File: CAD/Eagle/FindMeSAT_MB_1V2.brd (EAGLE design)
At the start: 99 x 49.2 mm, 135 parts, among them Q101 ABS07-32.768KHZ, Q651 ABM3B-16MHZ-10-R50-1-U, U1001 CFPT-141-20MHZ, U101 ATXMEGA256A3BU-AU, U1011 OPA354, U1021 OPA354, U1111 LM2831YMF, U1121 LM4120IM5-3.0, U201 SIM808, U301 MPU-9250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

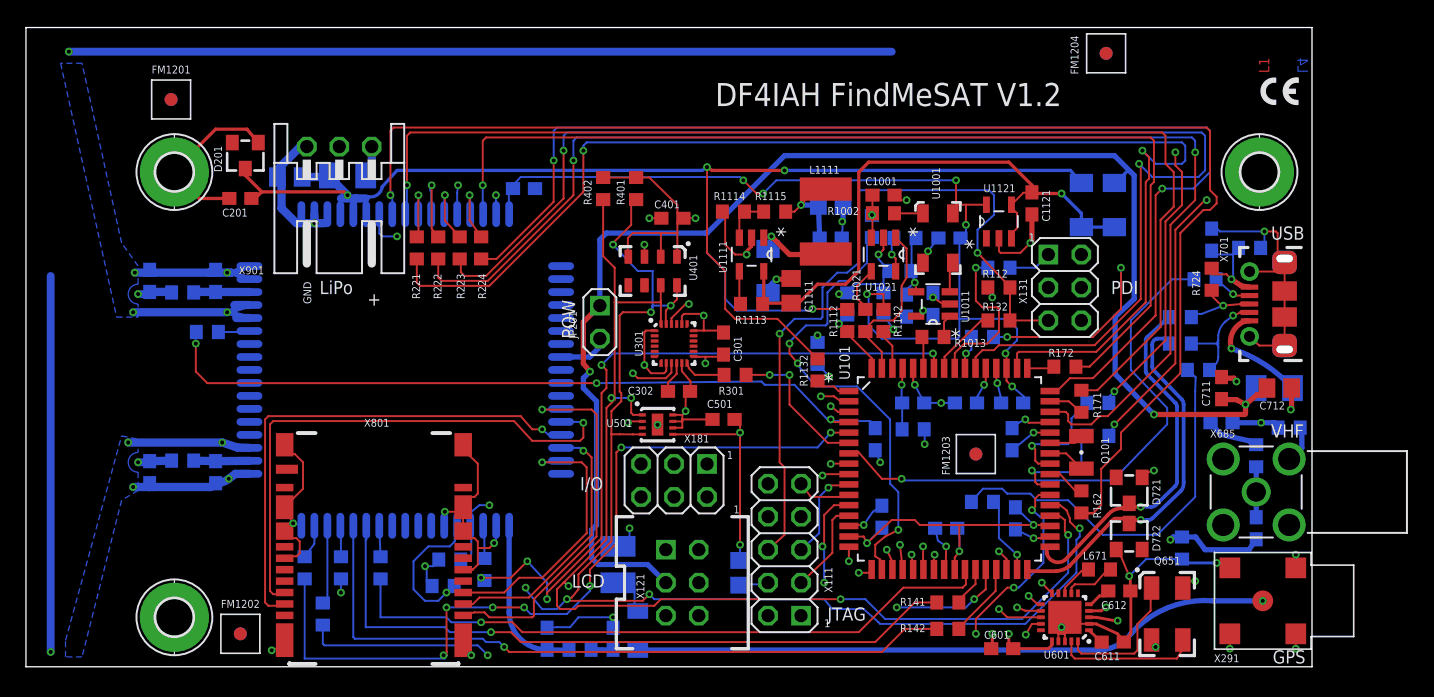
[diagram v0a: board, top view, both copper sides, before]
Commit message: HW_V1.2 - GSM antenna dimension (ADS), miter at busses, wire width in respect to 0.120 mm prepreg height - BT antenna still to do
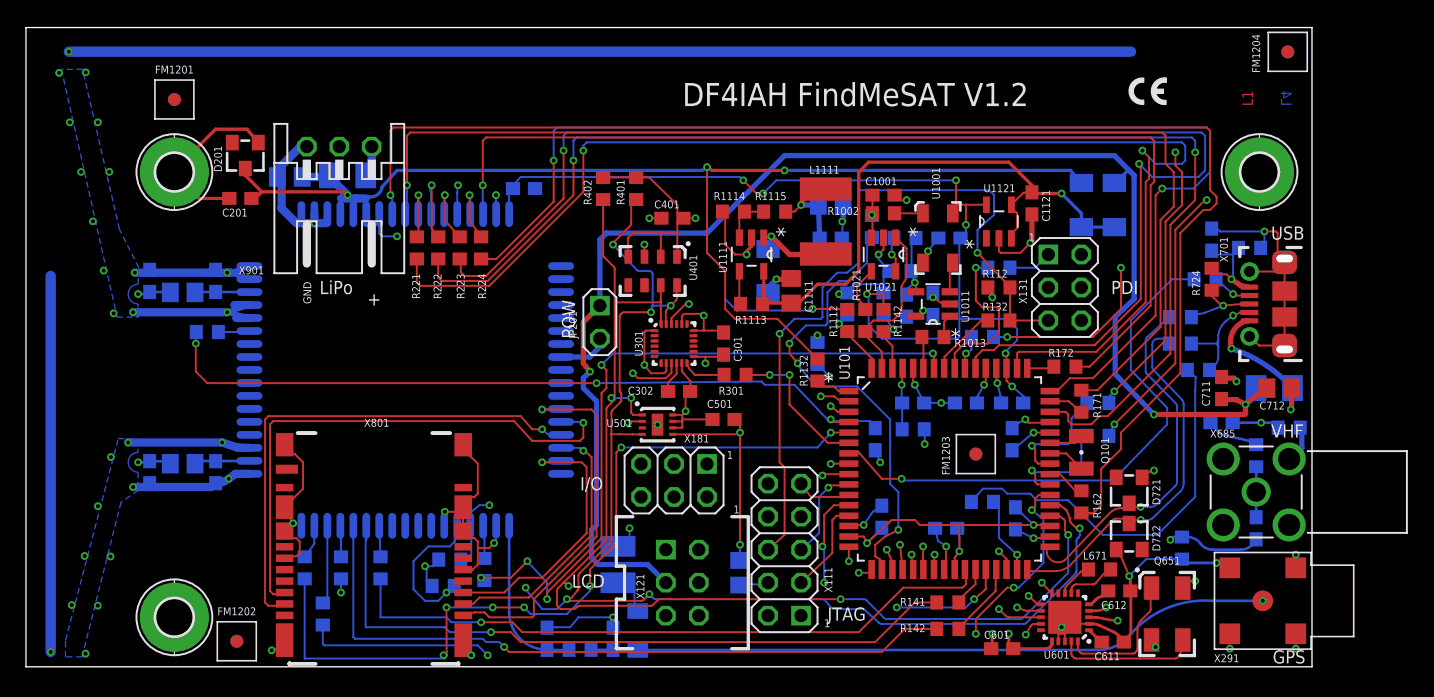
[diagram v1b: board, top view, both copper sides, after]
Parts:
- R271, R281: device rcl:R0603 -> rcl:R0805
- moved FM1204 14.0 mm to (97.2, 47.4)
- moved FM1202 0.64 mm to (16.2, 1.97)
- moved FM1201 0.25 mm to (11.4, 43.7)
- moved R281 0.24 mm to (12.1, 15.6)
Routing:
- net GSM_ANT: track 86.3 -> 104.8 mm
- net AX_CLK: track 14.4 -> 15.9 mm
- net SCL1: track 117.3 -> 116.4 mm
- net AX_ANTN: track 17.0 -> 16.5 mm
- net GND: vias 53 -> 69

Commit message: HW_V1.2 - GSM and BT antenna now without grounded arms
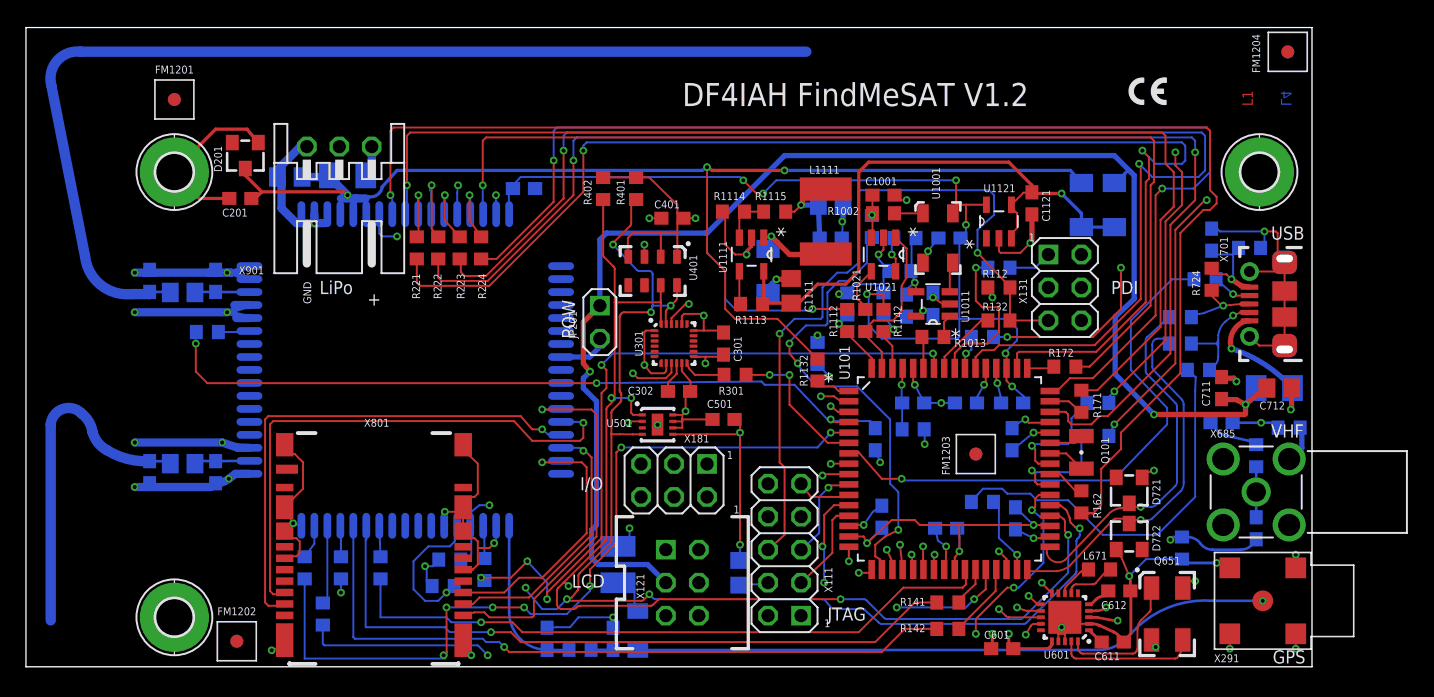
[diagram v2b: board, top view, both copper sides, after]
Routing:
- net GSM_ANT: track 104.8 -> 80.9 mm, vias 2 -> 0
- net BT_ANT: track 48.7 -> 26.2 mm, vias 2 -> 0
- net GND: track 233.1 -> 232.3 mm, vias 69 -> 53
- removed copper zone on layer 16, net GND
- removed copper zone on layer 2, net GND
- removed copper zone on layer 2, net SHIELD_BT
- removed copper zone on layer 2, net SHIELD_GSM

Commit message: HW_V1.2 - Eagle design made ready for the PCB board house
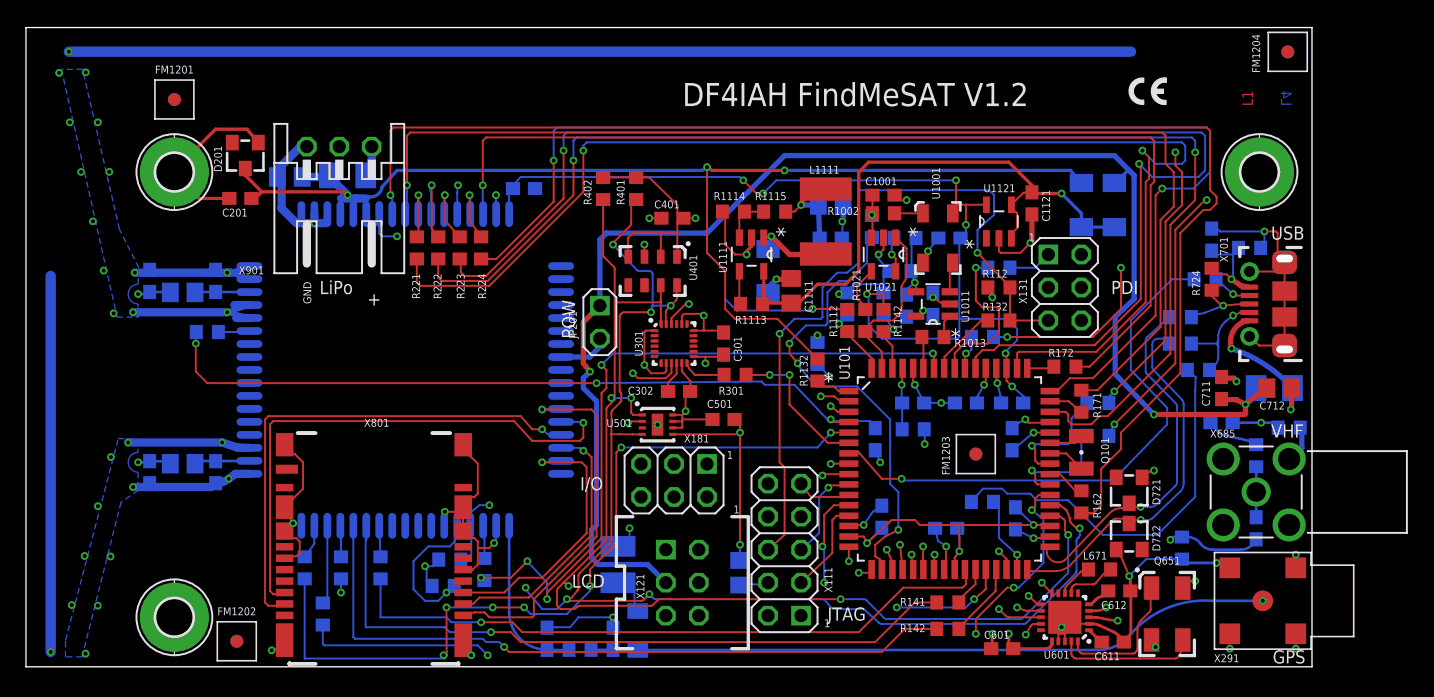
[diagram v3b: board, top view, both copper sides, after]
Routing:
- net GSM_ANT: track 80.9 -> 104.8 mm, vias 0 -> 2
- net BT_ANT: track 26.2 -> 48.7 mm, vias 0 -> 2
- net GND: track 232.3 -> 233.1 mm, vias 53 -> 69
- added copper zone on layer 16, net GND
- added copper zone on layer 2, net GND
- added copper zone on layer 2, net N$1
- added copper zone on layer 2, net N$2
- added copper zone on layer 2, net N$3
- added copper zone on layer 2, net N$4
- added copper zone on layer 2, net SHIELD_BT
- added copper zone on layer 2, net SHIELD_GSM

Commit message: HW_V1.2 - PWM low pass filter needs 10uF instead of 100nF, ADC measuring levels are 2.0V
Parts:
- C1001: value 100nF -> 10uF
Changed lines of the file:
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@@
 <attribute name="VALUE" x="71.755" y="31.115" size="1.27" layer="28" rot="MR0"/>
 </element>
-<element name="C1001" library="rcl" package="C0603" value="100nF" x="66.04" y="36.322" smashed="yes">
+<element name="C1001" library="rcl" package="C0603" value="10uF" x="66.04" y="36.322" smashed="yes">
 <attribute name="NAME" x="64.643" y="37.084" size="0.6096" layer="25"/>
 <attribute name="VALUE" x="65.278" y="35.941" size="0.6096" layer="27"/>

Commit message: HW_V1.2 - OPA354 needs higher comparator voltage for 50% duty cycle
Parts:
- R1012: value 470kR -> 270kR
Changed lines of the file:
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@@
 <attribute name="VALUE" x="69.469" y="27.432" size="0.6096" layer="28" rot="MR90"/>
 </element>
-<element name="R1012" library="rcl" package="R0603" value="470kR" x="67.691" y="33.02" smashed="yes" rot="MR0">
+<element name="R1012" library="rcl" package="R0603" value="270kR" x="67.691" y="33.02" smashed="yes" rot="MR0">
 <attribute name="NAME" x="68.961" y="33.909" size="0.6096" layer="26" rot="MR0"/>
 <attribute name="VALUE" x="68.453" y="32.766" size="0.6096" layer="28" rot="MR0"/>

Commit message: HW_V1.2 - Polyfuse of USB - value changed from 0.5A/1.0A to 1.1A/2.2A
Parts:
- RPOLY711: value 0.5A/1.0A -> 1.1A/2.2A
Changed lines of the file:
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@@
 <element name="H1203" library="holes" package="2,8-PAD" value="MOUNT-PAD-ROUND2.8" x="11.43" y="38.1" rot="R180"/>
 <element name="H1201" library="holes" package="2,8-PAD" value="MOUNT-PAD-ROUND2.8" x="94.996" y="38.1" smashed="yes" rot="R180"/>
-<element name="RPOLY711" library="rcl" package="M1206" value="0.5A/1.0A" x="96.139" y="21.463" smashed="yes" rot="MR0">
+<element name="RPOLY711" library="rcl" package="M1206" value="1.1A/2.2A" x="96.139" y="21.463" smashed="yes" rot="MR0">
 <attribute name="NAME" x="98.298" y="22.86" size="0.6096" layer="26" rot="MR0"/>
 <attribute name="VALUE" x="96.647" y="21.082" size="0.6096" layer="28" rot="MR0"/>

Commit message: HW_V1.2 - multiple missing fixes added (Hygro-Reset, R1141: 4.02kR --> 100pF, other value changes
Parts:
- R1012: value 270kR -> 330kR
- R1141: value 4.02kR -> 100pF
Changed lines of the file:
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@@
 <layer number="29" name="tStop" color="7" fill="3" visible="yes" active="yes"/>
 <layer number="30" name="bStop" color="7" fill="6" visible="yes" active="yes"/>
-<layer number="31" name="tCream" color="7" fill="4" visible="yes" active="yes"/>
-<layer number="32" name="bCream" color="7" fill="5" visible="yes" active="yes"/>
+<layer number="31" name="tCream" color="7" fill="4" visible="no" active="yes"/>
+<layer number="32" name="bCream" color="7" fill="5" visible="no" active="yes"/>
 <layer number="33" name="tFinish" color="6" fill="3" visible="no" active="yes"/>
 <layer number="34" name="bFinish" color="6" fill="6" visible="no" active="yes"/>
@@
 <attribute name="VALUE" x="69.469" y="27.432" size="0.6096" layer="28" rot="MR90"/>
 </element>
-<element name="R1012" library="rcl" package="R0603" value="270kR" x="67.691" y="33.02" smashed="yes" rot="MR0">
+<element name="R1012" library="rcl" package="R0603" value="330kR" x="67.691" y="33.02" smashed="yes" rot="MR0">
 <attribute name="NAME" x="68.961" y="33.909" size="0.6096" layer="26" rot="MR0"/>
 <attribute name="VALUE" x="68.453" y="32.766" size="0.6096" layer="28" rot="MR0"/>
@@
 <attribute name="VALUE" x="62.865" y="26.924" size="0.6096" layer="28" rot="MR90"/>
 </element>
-<element name="R1141" library="rcl" package="R0603" value="4.02kR" x="66.04" y="27.94" smashed="yes" rot="MR270">
+<element name="R1141" library="rcl" package="R0603" value="100pF" x="66.04" y="27.94" smashed="yes" rot="MR270">
 <attribute name="NAME" x="65.786" y="23.368" size="0.6096" layer="26" rot="MR90"/>
 <attribute name="VALUE" x="65.659" y="26.924" size="0.6096" layer="28" rot="MR90"/>

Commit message: HW_V1.2 - missing values for antenna matching circuits added
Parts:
- C271, C272, C281, C282, C291, C292: value (none) -> 0pF
- R271, R281, R291: value (none) -> 0R
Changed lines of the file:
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@@
 <attribute name="VALUE" x="32.131" y="32.004" size="0.6096" layer="27" rot="R90"/>
 </element>
-<element name="R271" library="rcl" package="R0805" value="" x="12.065" y="28.829" smashed="yes" rot="MR0">
+<element name="R271" library="rcl" package="R0805" value="0R" x="12.065" y="28.829" smashed="yes" rot="MR0">
 <attribute name="NAME" x="12.954" y="31.115" size="0.6096" layer="26" rot="MR0"/>
 <attribute name="VALUE" x="10.795" y="29.591" size="0.6096" layer="28" rot="MR90"/>
 </element>
-<element name="R281" library="rcl" package="R0805" value="" x="12.065" y="15.63958125" smashed="yes" rot="MR0">
+<element name="R281" library="rcl" package="R0805" value="0R" x="12.065" y="15.63958125" smashed="yes" rot="MR0">
 <attribute name="NAME" x="13.081" y="17.67158125" size="0.6096" layer="26" rot="MR0"/>
 <attribute name="VALUE" x="11.176" y="14.11558125" size="0.6096" layer="28" rot="MR0"/>
 </element>
-<element name="R291" library="rcl" package="R0603" value="" x="42.672" y="1.31" smashed="yes" rot="MR0">
+<element name="R291" library="rcl" package="R0603" value="0R" x="42.672" y="1.31" smashed="yes" rot="MR0">
 <attribute name="NAME" x="43.648" y="2.54" size="0.6096" layer="26" rot="MR0"/>
 <attribute name="VALUE" x="41.743" y="0.127" size="0.6096" layer="28" rot="MR0"/>
 </element>
-<element name="C291" library="rcl" package="C0603" value="" x="45.212" y="2.159" smashed="yes" rot="MR90">
+<element name="C291" library="rcl" package="C0603" value="0pF" x="45.212" y="2.159" smashed="yes" rot="MR90">
 <attribute name="NAME" x="45.466" y="3.81" size="0.6096" layer="26" rot="MR0"/>
 <attribute name="VALUE" x="44.069" y="2.54" size="0.6096" layer="28" rot="MR90"/>
 </element>
-<element name="C292" library="rcl" package="C0603" value="" x="40.132" y="2.159" smashed="yes" rot="MR90">
+<element name="C292" library="rcl" package="C0603" value="0pF" x="40.132" y="2.159" smashed="yes" rot="MR90">
 <attribute name="NAME" x="39.878" y="4.191" size="0.6096" layer="26" rot="MR90"/>
 <attribute name="VALUE" x="41.402" y="2.921" size="0.6096" layer="28" rot="MR270"/>
 </element>
-<element name="C271" library="rcl" package="C0603" value="" x="14.605" y="29.718" smashed="yes" rot="MR90">
+<element name="C271" library="rcl" package="C0603" value="0pF" x="14.605" y="29.718" smashed="yes" rot="MR90">
 <attribute name="NAME" x="14.351" y="31.496" size="0.6096" layer="26" rot="MR90"/>
 <attribute name="VALUE" x="13.335" y="30.099" size="0.6096" layer="28" rot="MR90"/>
 </element>
-<element name="C281" library="rcl" package="C0603" value="" x="14.605" y="14.986" smashed="yes" rot="MR270">
+<element name="C281" library="rcl" package="C0603" value="0pF" x="14.605" y="14.986" smashed="yes" rot="MR270">
 <attribute name="NAME" x="14.351" y="17.907" size="0.6096" layer="26" rot="MR90"/>
 <attribute name="VALUE" x="16.129" y="14.605" size="0.6096" layer="28" rot="MR270"/>
 </element>
-<element name="C272" library="rcl" package="C0603" value="" x="9.525" y="29.718" smashed="yes" rot="MR90">
+<element name="C272" library="rcl" package="C0603" value="0pF" x="9.525" y="29.718" smashed="yes" rot="MR90">
 <attribute name="NAME" x="9.271" y="31.496" size="0.6096" layer="26" rot="MR90"/>
 <attribute name="VALUE" x="10.922" y="29.337" size="0.6096" layer="28" rot="MR270"/>
 </element>
-<element name="C282" library="rcl" package="C0603" value="" x="9.525" y="14.986" smashed="yes" rot="MR270">
+<element name="C282" library="rcl" package="C0603" value="0pF" x="9.525" y="14.986" smashed="yes" rot="MR270">
 <attribute name="NAME" x="9.144" y="17.907" size="0.6096" layer="26" rot="MR90"/>
 <attribute name="VALUE" x="10.922" y="14.605" size="0.6096" layer="28" rot="MR270"/>
